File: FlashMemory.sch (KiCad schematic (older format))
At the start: 3 parts, among them U11 IS25WP256D-xM

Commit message: Small fix (#52)
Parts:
- C42: value C -> 100nF; footprint (none) -> Capacitor_SMD:C_0603_1608Metric_Pad1.05x0.95mm_HandSolder
- R33: footprint (none) -> Resistor_SMD:R_0603_1608Metric_Pad1.05x0.95mm_HandSolder
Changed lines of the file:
@@
 P 6000 1925
 F 0 "C42" H 6115 1971 50  0000 L CNN
-F 1 "C" H 6115 1880 50  0000 L CNN
-F 2 "" H 6038 1775 50  0001 C CNN
+F 1 "100nF" H 6115 1880 50  0000 L CNN
+F 2 "Capacitor_SMD:C_0603_1608Metric_Pad1.05x0.95mm_HandSolder" H 6038 1775 50  0001 C CNN
 F 3 "~" H 6000 1925 50  0001 C CNN
 	1    6000 1925
@@
 F 0 "R33" V 6550 2825 50  0000 C CNN
 F 1 "10K" V 6650 2825 50  0000 C CNN
-F 2 "" V 6580 2850 50  0001 C CNN
+F 2 "Resistor_SMD:R_0603_1608Metric_Pad1.05x0.95mm_HandSolder" V 6580 2850 50  0001 C CNN
 F 3 "~" H 6650 2850 50  0001 C CNN
 	1    6650 2850

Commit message: Ready To Go! (#53)
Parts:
- U11: Manufacturer (none) -> WINBOND; Part # (none) -> W25N01GVSFIT; VEND (none) -> MOUSER; VEND# (none) -> 454-W25N01GVSFIT
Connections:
- net HOLD: now reaches U11.1 (~HOLD~/IO3)
- net WP: now reaches U11.9 (~WP~/IO2)
- no-connect marks 2 -> 0
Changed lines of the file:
@@
 F 2 "Package_SO:SOIC-16W_7.5x10.3mm_P1.27mm" H 6050 3350 50  0001 C CNN
 F 3 "http://www.issi.com/WW/pdf/IS25LP(WP)256D.pdf" H 6050 2250 50  0001 C CNN
+F 4 "WINBOND" H 0   0   50  0001 C CNN "Manufacturer"
+F 5 "W25N01GVSFIT" H 0   0   50  0001 C CNN "Part #"
+F 6 "MOUSER" H 0   0   50  0001 C CNN "VEND"
+F 7 "454-W25N01GVSFIT" H 0   0   50  0001 C CNN "VEND#"
 	1    6000 2750
 	1    0    0    -1
@@
 Text HLabel 6000 2175 0    50   Input ~ 10
 VDD
-NoConn ~ 5500 2850
-NoConn ~ 5500 2950
 $Comp
 L Device:R R33
@@
 Text Label 6800 2850 0    50   ~ 10
 VDD
+Text HLabel 5500 2950 0    50   Input ~ 10
+HOLD
+Text HLabel 5500 2850 0    50   Input ~ 10
+WP
 $EndSCHEMATC

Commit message: from Ola and Jared (#71)
* Update

* removed fp-info-cache from git

* Gerbers

* moved connector

* Mostly Ola's e-mailed copy, plus some of my own fixes to his almost done revision. I also did some house cleaning, with boundary edges, removed most DRC and ERC errors, etc.

* added Fiducial's
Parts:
- C42: footprint Capacitor_SMD:C_0603_1608Metric_Pad1.05x0.95mm_HandSolder -> Capacitor_SMD:C_0603_1608Metric
- R33: footprint Resistor_SMD:R_0603_1608Metric_Pad1.05x0.95mm_HandSolder -> Resistor_SMD:R_0603_1608Metric
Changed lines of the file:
@@
 EELAYER 29 0
 EELAYER END
-$Descr A4 11693 8268
+$Descr A 11000 8500
 encoding utf-8
 Sheet 7 7
-Title ""
-Date ""
-Rev ""
+Title "microRusEfi"
+Date "2019-07-01"
+Rev "R0.2"
 Comp ""
 Comment1 ""
@@
 F 0 "C42" H 6115 1971 50  0000 L CNN
 F 1 "100nF" H 6115 1880 50  0000 L CNN
-F 2 "Capacitor_SMD:C_0603_1608Metric_Pad1.05x0.95mm_HandSolder" H 6038 1775 50  0001 C CNN
+F 2 "Capacitor_SMD:C_0603_1608Metric" H 6038 1775 50  0001 C CNN
 F 3 "~" H 6000 1925 50  0001 C CNN
 	1    6000 1925
@@
 F 0 "R33" V 6550 2825 50  0000 C CNN
 F 1 "10K" V 6650 2825 50  0000 C CNN
-F 2 "Resistor_SMD:R_0603_1608Metric_Pad1.05x0.95mm_HandSolder" V 6580 2850 50  0001 C CNN
+F 2 "Resistor_SMD:R_0603_1608Metric" V 6580 2850 50  0001 C CNN
 F 3 "~" H 6650 2850 50  0001 C CNN
 	1    6650 2850

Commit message: Updated logo symbol and footprint, BOM is 99% entered in KC schematic now.
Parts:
- C42: Manufacturer (none) -> KEMET; Part # (none) -> C0603C104J5RACTU; VEND (none) -> DIGI; VEND# (none) -> 399-7844-1-ND
- R33: Manufacturer (none) -> StackPole; Part # (none) -> RMCF0603JT10K0; VEND (none) -> DIGI; VEND# (none) -> RMCF0603JT10K0CT-ND
- U11: Manufacturer WINBOND -> ISSI; Part # W25N01GVSFIT -> IS25WP256D-RMLE; VEND MOUSER -> DIGI; VEND# 454-W25N01GVSFIT -> 706-1654-ND
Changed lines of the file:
@@
 F 2 "Package_SO:SOIC-16W_7.5x10.3mm_P1.27mm" H 6050 3350 50  0001 C CNN
 F 3 "http://www.issi.com/WW/pdf/IS25LP(WP)256D.pdf" H 6050 2250 50  0001 C CNN
-F 4 "WINBOND" H 0   0   50  0001 C CNN "Manufacturer"
-F 5 "W25N01GVSFIT" H 0   0   50  0001 C CNN "Part #"
-F 6 "MOUSER" H 0   0   50  0001 C CNN "VEND"
-F 7 "454-W25N01GVSFIT" H 0   0   50  0001 C CNN "VEND#"
+F 4 "ISSI" H 0   0   50  0001 C CNN "Manufacturer"
+F 5 "IS25WP256D-RMLE" H 0   0   50  0001 C CNN "Part #"
+F 6 "DIGI" H 0   0   50  0001 C CNN "VEND"
+F 7 "706-1654-ND" H 0   0   50  0001 C CNN "VEND#"
 	1    6000 2750
 	1    0    0    -1
@@
 F 2 "Capacitor_SMD:C_0603_1608Metric" H 6038 1775 50  0001 C CNN
 F 3 "~" H 6000 1925 50  0001 C CNN
+F 4 "C0603C104J5RACTU" H 0   0   50  0001 C CNN "Part #"
+F 5 "DIGI" H 0   0   50  0001 C CNN "VEND"
+F 6 "399-7844-1-ND" H 0   0   50  0001 C CNN "VEND#"
+F 7 "KEMET" H 0   0   50  0001 C CNN "Manufacturer"
 	1    6000 1925
 	1    0    0    -1
@@
 F 2 "Resistor_SMD:R_0603_1608Metric" V 6580 2850 50  0001 C CNN
 F 3 "~" H 6650 2850 50  0001 C CNN
+F 4 "RMCF0603JT10K0" H 0   0   50  0001 C CNN "Part #"
+F 5 "DIGI" H 0   0   50  0001 C CNN "VEND"
+F 6 "RMCF0603JT10K0CT-ND" H 0   0   50  0001 C CNN "VEND#"
+F 7 "StackPole" H 0   0   50  0001 C CNN "Manufacturer"
 	1    6650 2850
 	0    1    1    0

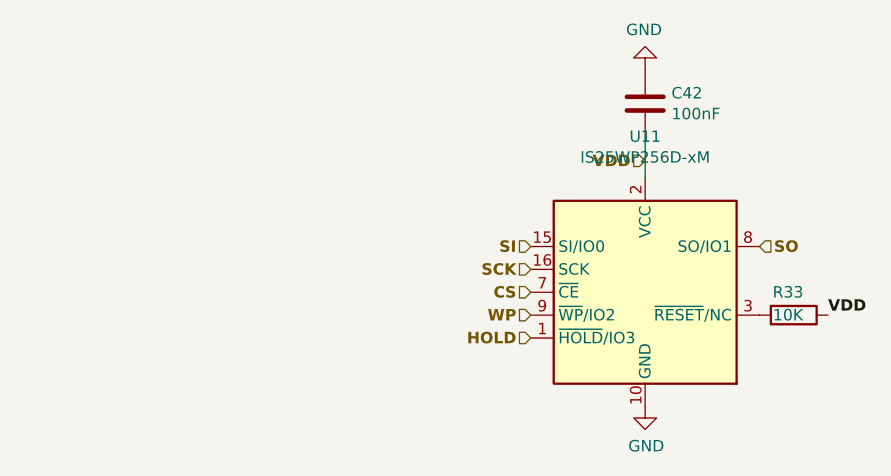
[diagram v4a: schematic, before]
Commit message: Updated 1k/1.5k resistor arrays, updated 2.7k's and R141. Changed several K's into k's for consistent ref designation names. https://github.com/rusefi/hw_microRusEfi/issues/51
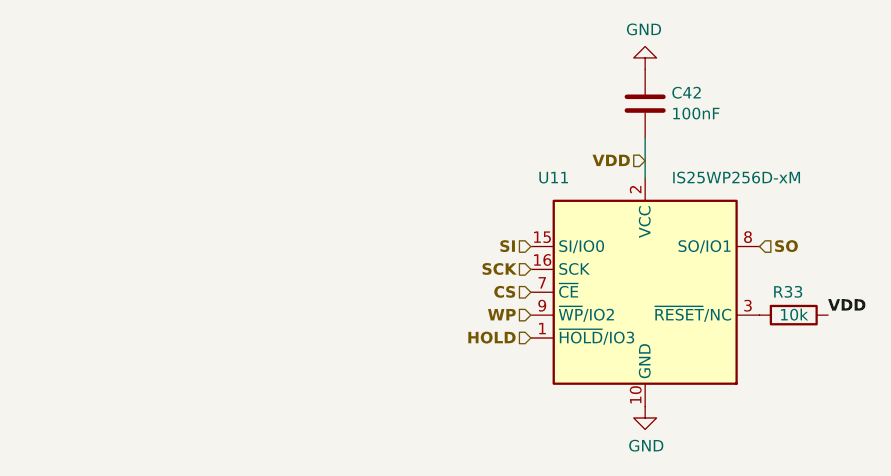
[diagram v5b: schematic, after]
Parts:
- R33: value 10K -> 10k
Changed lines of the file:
@@
 U 1 1 5D2F2515
 P 6000 2750
-F 0 "U11" H 6000 3431 50  0000 C CNN
-F 1 "IS25WP256D-xM" H 6000 3340 50  0000 C CNN
+F 0 "U11" H 5600 3250 50  0000 C CNN
+F 1 "IS25WP256D-xM" H 6400 3250 50  0000 C CNN
 F 2 "Package_SO:SOIC-16W_7.5x10.3mm_P1.27mm" H 6050 3350 50  0001 C CNN
 F 3 "http://www.issi.com/WW/pdf/IS25LP(WP)256D.pdf" H 6050 2250 50  0001 C CNN
@@
 P 6650 2850
 F 0 "R33" V 6550 2825 50  0000 C CNN
-F 1 "10K" V 6650 2825 50  0000 C CNN
+F 1 "10k" V 6650 2850 50  0000 C CNN
 F 2 "Resistor_SMD:R_0603_1608Metric" V 6580 2850 50  0001 C CNN
-F 3 "~" H 6650 2850 50  0001 C CNN
+F 3 "TBD" H 6650 2850 50  0001 C CNN
 F 4 "RMCF0603JT10K0" H 0   0   50  0001 C CNN "Part #"
 F 5 "DIGI" H 0   0   50  0001 C CNN "VEND"

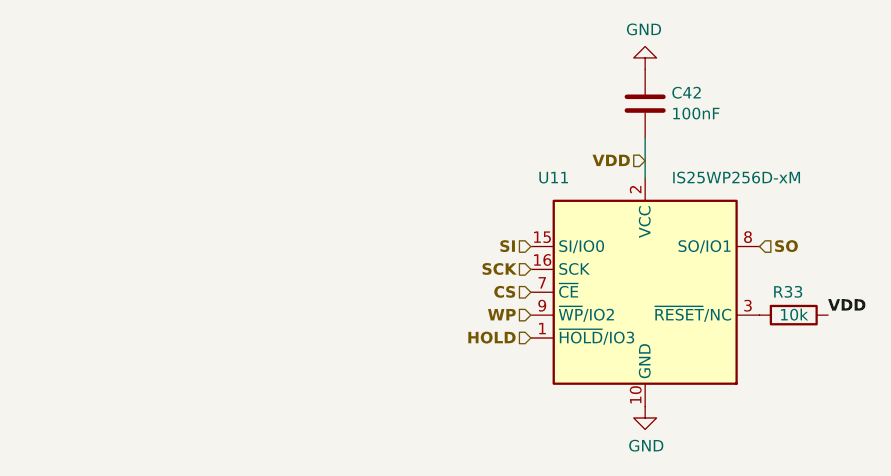
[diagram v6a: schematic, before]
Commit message: Re-worked layout, wider traces, segregated ground current, opened area (#110)
* Add files via upload

* cover bolt info from stefanst

* Re-organized top vs bottom components.  Fixed footprint

* Moved GP5/6 voltage selection to center.

* Significant revision of schematic and layout:

Added reverse voltage protection.
Split 12V supply into a 12V-Key (ignition) pin and a 12V-MRel (supply from
main relay) pin.  The 12V main relay is controlled by the MRel pin to protect against reverse voltage and over-voltage.

The board can optionally draw under 1mA from the main relay coil to power
standby features, including CAN monitoring.

Increased the size of several resistors, notably ignition output resistors
and CAN termination, to handle typical power draw.

Changed resistor dividers to individual resistors for better accuracy than
typical resistor networks.

Standardized pull-up and pull-down resistors to 10K.

Changed to a tab-output regulator.

* Includes all known errata, except for component rotation for JLCPCB fabrication.

Includes
  Refined reverse protection layout with dual SS54 diodes
  Load dump protection, SMB TVS for 33V TVS
  Multiple footprints for Flash (SO-16, SO-8-208 and SO-8-150)
  Simplified pull-up and pull-down resistors, omitting unneeded ones
  Individual resistors for resistor dividers for easier sourcing of
    1% precision (most resistor networks are 5%, most 0603 parts are 1%).
  PicoBlade connector for RTC battery, matches low-cost laptop 2032 cells
  Clamping diode arrays on top, alternate BAS70 on bottom
  Options for VR input modification, and analog pull-ups on bottom.
  LM1117 voltage regulator footprint

* Added 2x5 header for SPI/serial communications
Connected LIN to PD8/PD9 USART3, output on SMD testpoint.
Added standby regulator.
Changed footprints of reverse protection diodes to SMA.
Rotated two opamps and clamping diode arrays for cleaner layout.
Moved status LEDs over for better silk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
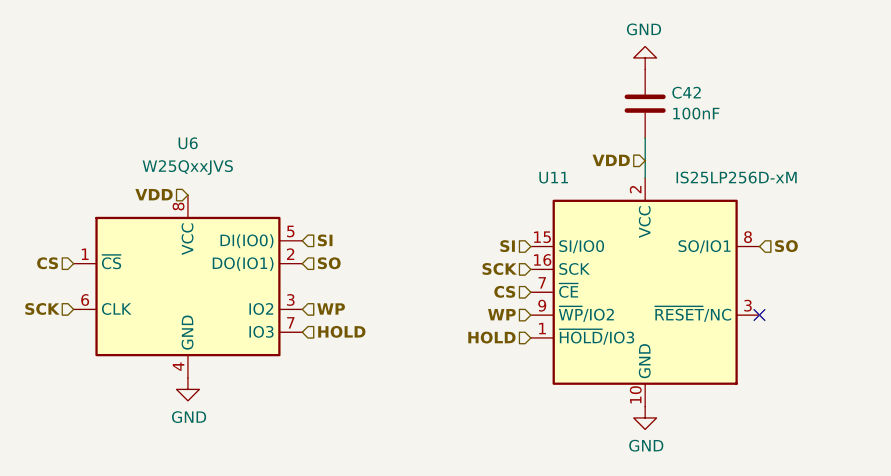
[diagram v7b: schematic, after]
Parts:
- removed R33: 10k, Resistor_SMD:R_0603_1608Metric, symbol Device:R
- added U6: W25QxxJVS, hw_microRusEfi-master:SO-8_5.3x6.2mm_P1.27mm-150+208, symbol Memory_Flash:W25Q32JVSS
- C42: LCSC (none) -> C14663
- U11: value IS25WP256D-xM -> IS25LP256D-xM; Part # IS25WP256D-RMLE -> IS25LP256D-RMLE; VEND DIGI -> (none); VEND# 706-1654-ND -> (none)
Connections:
- net CS: now also U6.1 (~CS)
- net GND: now also U6.4 (GND)
- net HOLD: now also U6.7 (IO3)
- net SCK: now also U6.6 (CLK)
- net SI: now also U6.5 (DI(IO0))
- net SO: now also U6.2 (DO(IO1))
- net VDD: now also U6.8 (VCC)
- net WP: now also U6.3 (IO2)
- no-connect marks 0 -> 1
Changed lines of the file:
@@
 $Descr A 11000 8500
 encoding utf-8
-Sheet 7 7
-Title "microRusEfi"
-Date "2019-07-01"
-Rev "R0.2"
-Comp ""
-Comment1 ""
+Sheet 6 7
+Title "microRusEfi-2L"
+Date "2019-10-08"
+Rev "R0.4.5"
+Comp "rusEFI.com"
+Comment1 "Donald Becker"
 Comment2 ""
 Comment3 ""
@@
 P 6000 2750
 F 0 "U11" H 5600 3250 50  0000 C CNN
-F 1 "IS25WP256D-xM" H 6400 3250 50  0000 C CNN
+F 1 "IS25LP256D-xM" H 6400 3250 50  0000 C CNN
 F 2 "Package_SO:SOIC-16W_7.5x10.3mm_P1.27mm" H 6050 3350 50  0001 C CNN
 F 3 "http://www.issi.com/WW/pdf/IS25LP(WP)256D.pdf" H 6050 2250 50  0001 C CNN
 F 4 "ISSI" H 0   0   50  0001 C CNN "Manufacturer"
-F 5 "IS25WP256D-RMLE" H 0   0   50  0001 C CNN "Part #"
-F 6 "DIGI" H 0   0   50  0001 C CNN "VEND"
-F 7 "706-1654-ND" H 0   0   50  0001 C CNN "VEND#"
+F 5 "IS25LP256D-RMLE" H 0   0   50  0001 C CNN "Part #"
 	1    6000 2750
 	1    0    0    -1
@@
 F 6 "399-7844-1-ND" H 0   0   50  0001 C CNN "VEND#"
 F 7 "KEMET" H 0   0   50  0001 C CNN "Manufacturer"
+F 8 "C14663" H 6000 1925 50  0001 C CNN "LCSC"
 	1    6000 1925
 	1    0    0    -1
@@
 Text HLabel 6000 2175 0    50   Input ~ 10
 VDD
-$Comp
-L Device:R R33
-U 1 1 5D2F5EFA
-P 6650 2850
-F 0 "R33" V 6550 2825 50  0000 C CNN
-F 1 "10k" V 6650 2850 50  0000 C CNN
-F 2 "Resistor_SMD:R_0603_1608Metric" V 6580 2850 50  0001 C CNN
-F 3 "TBD" H 6650 2850 50  0001 C CNN
-F 4 "RMCF0603JT10K0" H 0   0   50  0001 C CNN "Part #"
-F 5 "DIGI" H 0   0   50  0001 C CNN "VEND"
-F 6 "RMCF0603JT10K0CT-ND" H 0   0   50  0001 C CNN "VEND#"
-F 7 "StackPole" H 0   0   50  0001 C CNN "Manufacturer"
-	1    6650 2850
-	0    1    1    0
-$EndComp
-Text Label 6800 2850 0    50   ~ 10
-VDD
 Text HLabel 5500 2950 0    50   Input ~ 10
 HOLD
 Text HLabel 5500 2850 0    50   Input ~ 10
 WP
+$Comp
+L Memory_Flash:W25Q32JVSS U6
+U 1 1 5E09CE64
+P 4000 2725
+F 0 "U6" H 4000 3350 50  0000 C CNN
+F 1 "W25QxxJVS" H 4000 3250 50  0000 C CNN
+F 2 "hw_microRusEfi-master:SO-8_5.3x6.2mm_P1.27mm-150+208" H 4000 2725 50  0001 C CNN
+F 3 "http://www.winbond.com/resource-files/w25q32jv%20revg%2003272018%20plus.pdf" H 4000 2725 50  0001 C CNN
+F 4 "C97521" H 4000 2725 50  0001 C CNN "LCSC"
+	1    4000 2725
+	1    0    0    -1
+$EndComp
+Text HLabel 3500 2825 0    50   Input ~ 10
+SCK
+Text HLabel 3500 2625 0    50   Input ~ 10
+CS
+Text HLabel 4500 2825 2    50   Input ~ 10
+WP
+Text HLabel 4500 2925 2    50   Input ~ 10
+HOLD
+Text HLabel 4500 2625 2    50   Input ~ 10
+SO
+Text HLabel 4500 2525 2    50   Input ~ 10
+SI
+Text HLabel 4000 2325 0    50   Input ~ 10
+VDD
+$Comp
+L power:GND #PWR024
+U 1 1 5E148347
+P 4000 3125
+F 0 "#PWR024" H 4000 2875 50  0001 C CNN
+F 1 "GND" H 4005 2952 50  0000 C CNN
+F 2 "" H 4000 3125 50  0001 C CNN
+F 3 "" H 4000 3125 50  0001 C CNN
+	1    4000 3125
+	1    0    0    -1
+$EndComp
+NoConn ~ 6500 2850
 $EndSCHEMATC
